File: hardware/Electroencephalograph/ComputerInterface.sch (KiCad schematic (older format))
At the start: 15 parts, among them J5 USB_B_Micro, U6 FT200XD

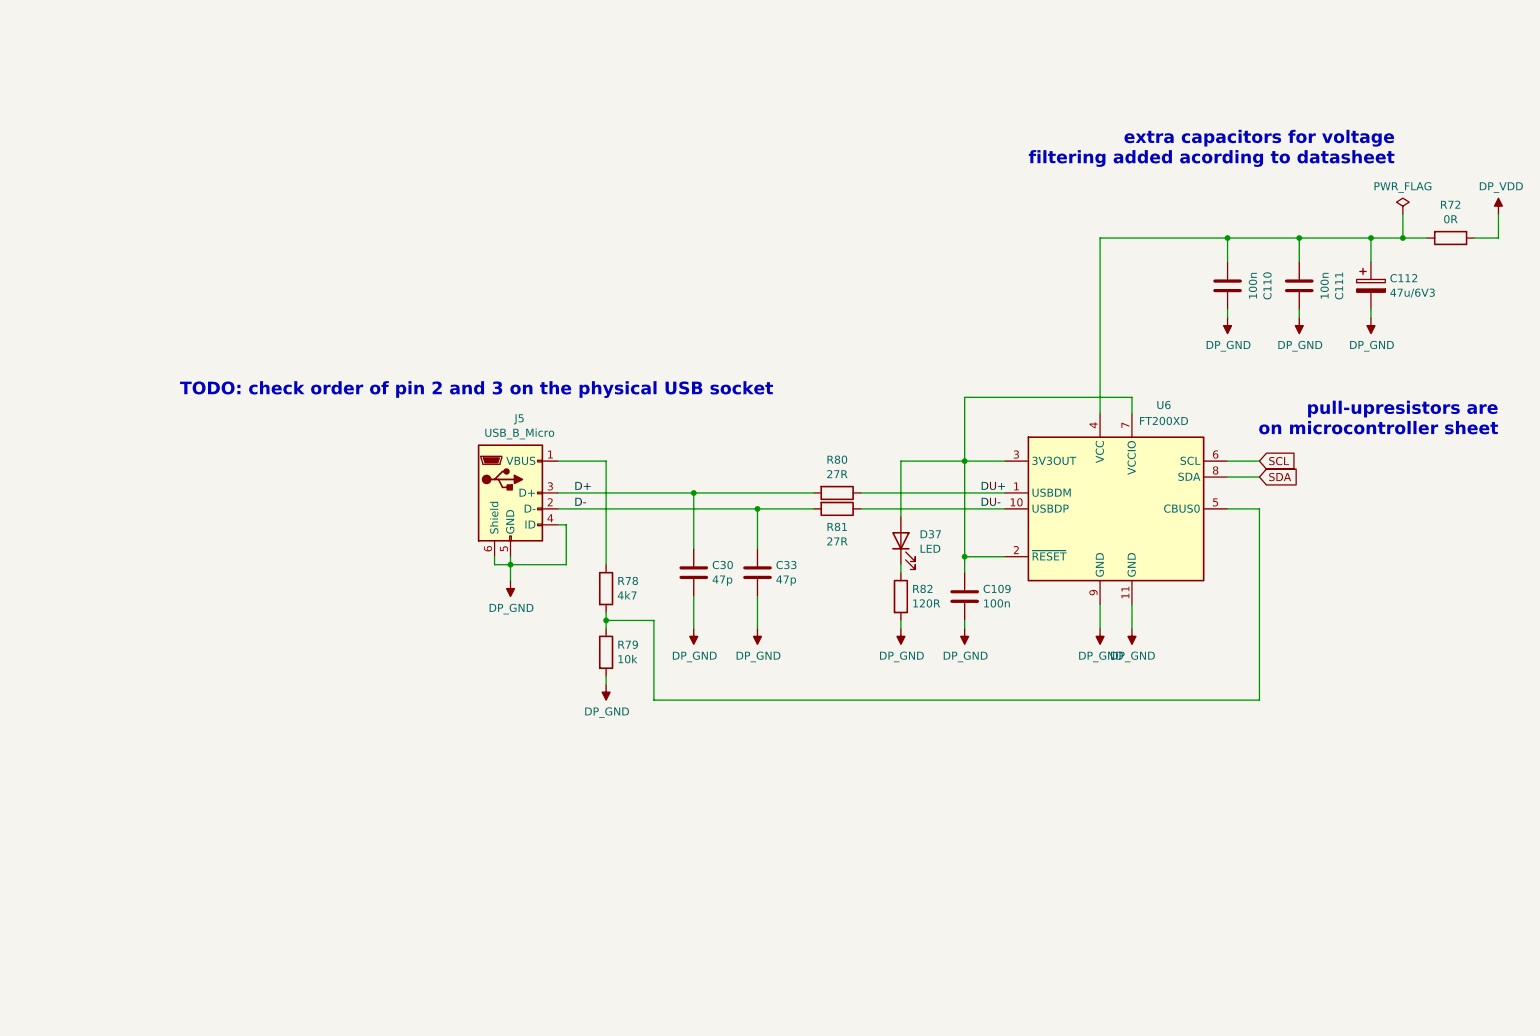
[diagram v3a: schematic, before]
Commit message: add support for esp module
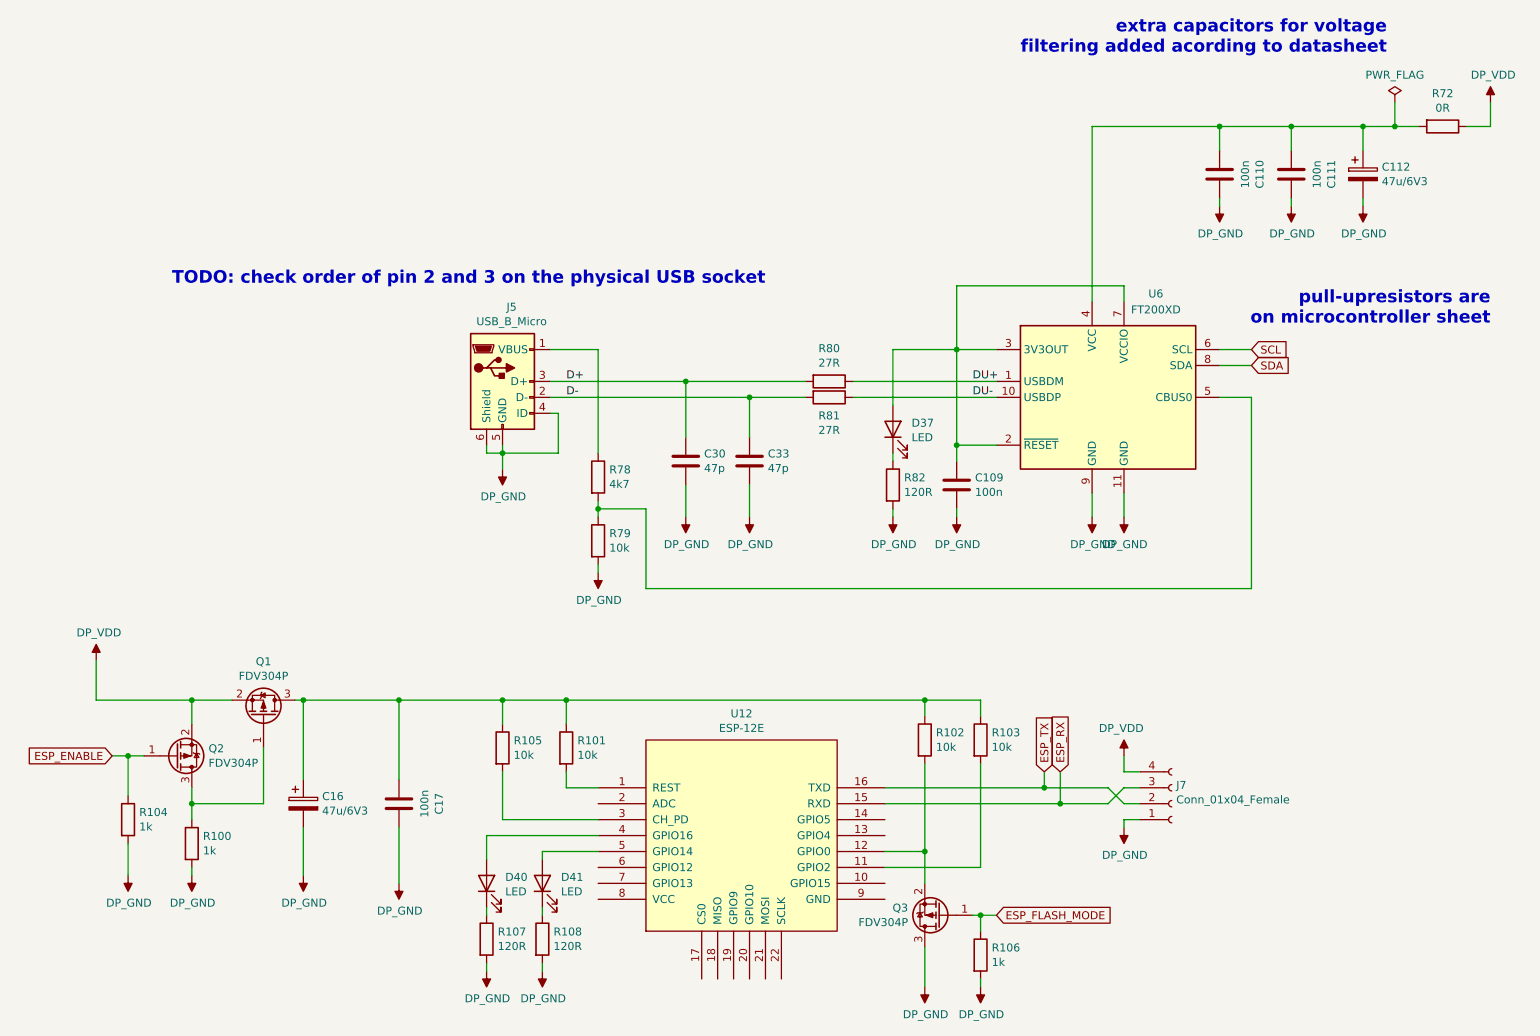
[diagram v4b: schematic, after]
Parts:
- added C16: 47u/6V3, Capacitor_Tantalum_SMD:CP_EIA-3528-21_Kemet-B, symbol Device:CP
- added C17: 100n, Capacitor_SMD:C_0402_1005Metric, symbol Device:C
- added D40, D41: LED, LED_SMD:LED_0402_1005Metric, symbol Device:LED
- added J7: Conn_01x04_Female, Connector_PinHeader_2.54mm:PinHeader_1x04_P2.54mm_Vertical, symbol Connector:Conn_01x04_Female
- added Q1, Q2, Q3: FDV304P, Package_TO_SOT_SMD:SOT-23, symbol Device:Q_PMOS_GSD
- added R100, R104, R106: 1k, Resistor_SMD:R_0402_1005Metric, symbol Device:R
- added R101, R102, R103, R105: 10k, Resistor_SMD:R_0402_1005Metric, symbol Device:R
- added R107, R108: 120R, Resistor_SMD:R_0402_1005Metric, symbol Device:R
- added U12: ESP-12E, ESP8266:ESP-12E, symbol ESP8266:ESP-12E
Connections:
- net DP_GND: now also C16.2, C17.2, J7.1 (Pin_1), Q3.3 (D), R100.2, R104.2, R106.2, R107.2, R108.2
- net DP_VDD: now also J7.4 (Pin_4), Q1.2 (S), Q2.2 (S)
- new net: R101.2, U12.1 (REST)
- new net: R103.2, U12.11 (GPIO2)
- new net: Q3.2 (S), R102.2, U12.12 (GPIO0)
- new net: R105.2, U12.3 (CH_PD)
- new net: D40.2 (A), U12.4 (GPIO16)
- new net: D41.2 (A), U12.5 (GPIO14)
- new net: C16.1, C17.1, Q1.3 (D), R101.1, R102.1, R103.1, R105.1
- new net: Q1.1 (G), Q2.3 (D), R100.1
- new net: D40.1 (K), R107.1
- new net: D41.1 (K), R108.1
- new net ESP_ENABLE: Q2.1 (G), R104.1
- new net ESP_FLASH_MODE: Q3.1 (G), R106.1
- new net ESP_RX: J7.3 (Pin_3), U12.15 (RXD)
- new net ESP_TX: J7.2 (Pin_2), U12.16 (TXD)
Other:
- moved on the sheet: C109, C110, C111, C112, C30, C33, D37, J5, R72, R78, R79, R80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
